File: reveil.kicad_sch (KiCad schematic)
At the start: 24 parts, among them J1 Barrel_Jack_Switch, J2 AudioJack3_SwitchTR, M1 Motor_DC, Q1 2N3904, Q2 IRLB8721PBF

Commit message: Schéma/PCB : isole VBUS du jack J1, alimente le reste de la carte via VSYS
Le jack J1 alimentait directement le net VBUS, partagé avec la broche VBUS
du Pico : branché en même temps que l'USB, les deux 5 V se retrouvaient en
parallèle et le jack pouvait renvoyer du courant vers le PC.

Ajoute D3 (Schottky 1N5822, même référence que D2) entre le jack et un
nouveau rail renommé VSYS, plus C6 (220 µF) en entrée. Tout ce qui était
sur VBUS (MAX7219 U1/U2, moteur, LED, D2) passe sur VSYS, qui alimente le
Pico via sa broche VSYS (39) au lieu de VBUS (40) — VBUS reste réservé à
l'alimentation USB du Pico lui-même.

Met à jour le README (TODO alimentation + table des points de test).

Co-Authored-By: Claude Sonnet 5 <noreply@anthropic.com>
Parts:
- added C6: 220uF, Capacitor_THT:CP_Radial_D7.5mm_P2.50mm, symbol Device:C_Polarized
- added D3: 1N5822, Diode_THT:D_DO-41_SOD81_P10.16mm_Horizontal, symbol Device:D_Schottky
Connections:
- net GND: now also C6.2
- net VSYS: now reaches A1.39 (VSYS)
- net VSYS: now also C5.1, D1.2 (A), D2.1 (K), J2.S, M1.1 (+), C6.1, D3.1 (K)
- removed net VBUS: A1.40 (VBUS), C5.1, D1.2 (A), D2.1 (K), J1.1, J2.S, M1.1 (+)
- new net: D3.2 (A), J1.1

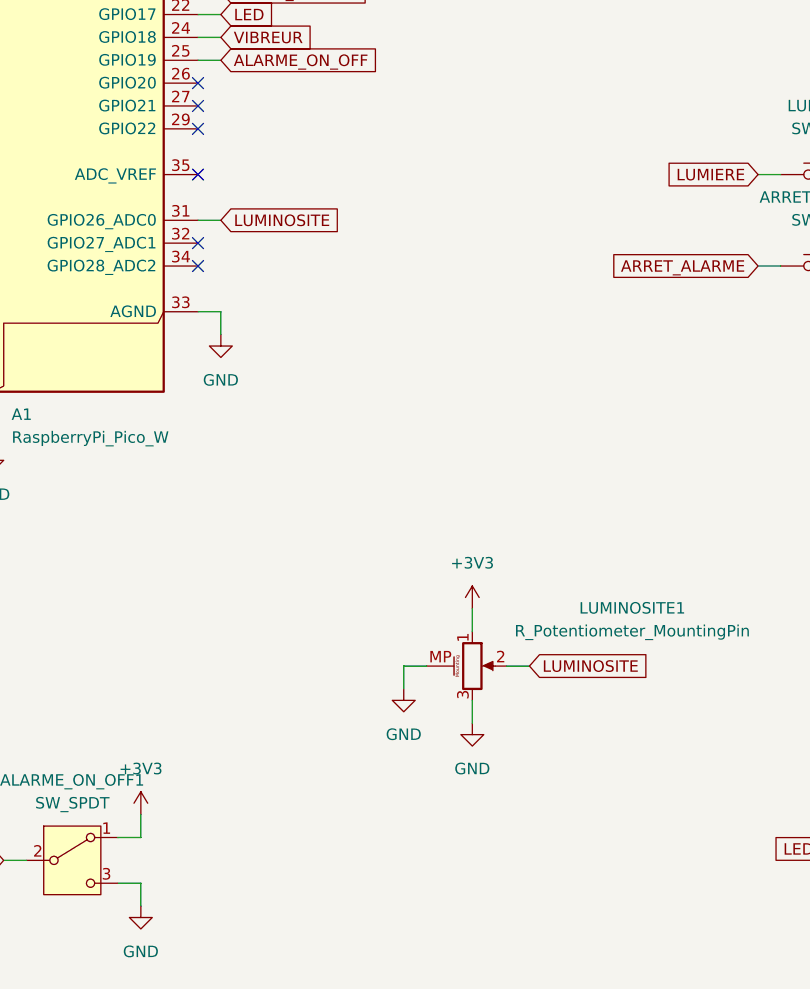
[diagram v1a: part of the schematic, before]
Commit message: Schéma/PCB : découple LUMINOSITE et l'alimente depuis ADC_VREF
Ajoute C7 (100 nF) sur le curseur du potentiomètre LUMINOSITE1, et
reconnecte le haut du pont diviseur sur la broche ADC_VREF du Pico
(auparavant non connectée) au lieu de +3V3, pour une référence ADC plus
propre.

Met à jour le README : coche ce point, et marque le bouton reset et les
filtres RC des encodeurs comme des décisions explicites (pas voulus /
pas nécessaires pour l'instant) plutôt que des TODO ouverts.

Co-Authored-By: Claude Sonnet 5 <noreply@anthropic.com>
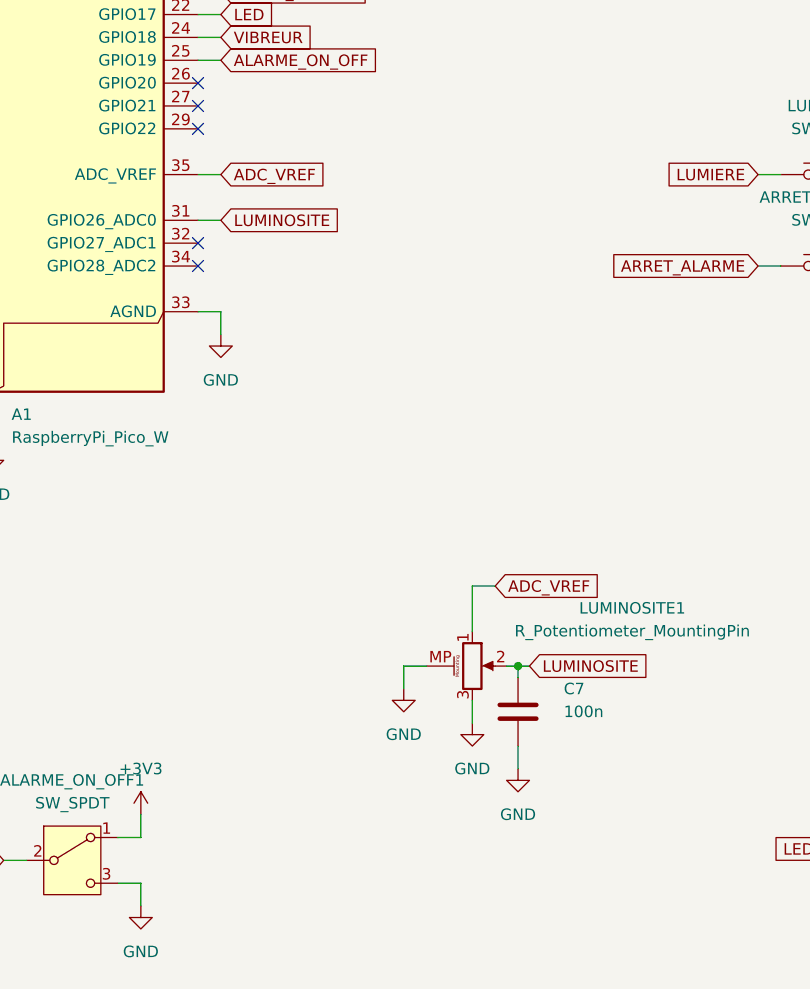
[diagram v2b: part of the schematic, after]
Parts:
- added C7: 100n, Capacitor_THT:C_Disc_D3.0mm_W1.6mm_P2.50mm, symbol Device:C
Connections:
- net +3V3: no longer LUMINOSITE1.1
- net GND: now also C7.2
- net LUMINOSITE: now also C7.1
- net ADC_VREF: now reaches A1.35 (ADC_VREF)
- net ADC_VREF: now also LUMINOSITE1.1
- no-connect marks 13 -> 12
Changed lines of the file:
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@@
 	)
 	(junction
+		(at 140.97 123.19)
+		(diameter 0)
+		(color 0 0 0 0)
+	)
+	(junction
 		(at 185.42 143.51)
 		(diameter 0)
@@
 	)
 	(no_connect
-		(at 105.41 68.58)
-	)
-	(no_connect
 		(at 105.41 60.96)
 	)
@@
 	(wire
 		(pts
+			(xy 105.41 68.58) (xy 107.95 68.58)
+		)
+		(stroke
+			(width 0)
+			(type default)
+		)
+	)
+	(wire
+		(pts
 			(xy 165.1 35.56) (xy 170.18 35.56)
 		)
@@
 	(wire
 		(pts
+			(xy 138.43 114.3) (xy 135.89 114.3)
+		)
+		(stroke
+			(width 0)
+			(type default)
+		)
+	)
+	(wire
+		(pts
 			(xy 233.68 35.56) (xy 238.76 35.56)
 		)
@@
 	(wire
 		(pts
-			(xy 142.24 123.19) (xy 139.7 123.19)
+			(xy 142.24 123.19) (xy 140.97 123.19)
 		)
 		(stroke
@@
 	(wire
 		(pts
+			(xy 135.89 114.3) (xy 135.89 119.38)
+		)
+		(stroke
+			(width 0)
+			(type default)
+		)
+	)
+	(wire
+		(pts
 			(xy 247.65 137.16) (xy 262.89 137.16)
 		)
@@
 	(wire
 		(pts
+			(xy 140.97 123.19) (xy 139.7 123.19)
+		)
+		(stroke
+			(width 0)
+			(type default)
+		)
+	)
+	(wire
+		(pts
 			(xy 254 35.56) (xy 259.08 35.56)
 		)
@@
 	(wire
 		(pts
+			(xy 140.97 132.08) (xy 140.97 134.62)
+		)
+		(stroke
+			(width 0)
+			(type default)
+		)
+	)
+	(wire
+		(pts
 			(xy 57.15 83.82) (xy 59.69 83.82)
 		)
@@
 	(wire
 		(pts
-			(xy 273.05 132.08) (xy 273.05 137.16)
+			(xy 140.97 123.19) (xy 140.97 124.46)
 		)
 		(stroke
@@
 	(wire
 		(pts
-			(xy 57.15 48.26) (xy 59.69 48.26)
+			(xy 273.05 132.08) (xy 273.05 137.16)
 		)
 		(stroke
@@
 	(wire
 		(pts
-			(xy 107.95 55.88) (xy 105.41 55.88)
+			(xy 57.15 48.26) (xy 59.69 48.26)
 		)
 		(stroke
@@
 	(wire
 		(pts
-			(xy 135.89 116.84) (xy 135.89 119.38)
+			(xy 107.95 55.88) (xy 105.41 55.88)
 		)
 		(stroke
@@
 		)
 	)
+	(global_label "ADC_VREF"
+		(shape input)
+		(at 138.43 114.3 0)
+		(fields_autoplaced yes)
+		(effects
+			(font
+				(size 1.27 1.27)
+			)
+			(justify left)
+		)
+		(property "Intersheetrefs" "${INTERSHEET_REFS}"
+			(at 150.6076 114.3 0)
+			(effects
+				(font
+					(size 1.27 1.27)
+				)
+				(justify left)
+				(hide yes)
+			)
+		)
+	)
 	(global_label "HEURE_ALARME_DIN"
 		(shape input)
@@
 		)
 	)
+	(global_label "ADC_VREF"
+		(shape input)
+		(at 107.95 68.58 0)
+		(fields_autoplaced yes)
+		(effects
+			(font
+				(size 1.27 1.27)
+			)
+			(justify left)
+		)
+		(property "Intersheetrefs" "${INTERSHEET_REFS}"
+			(at 120.1276 68.58 0)
+			(effects
+				(font
+					(size 1.27 1.27)
+				)
+				(justify left)
+				(hide yes)
+			)
+		)
+	)
 	(global_label "REGLAGE_DATE_A"
 		(shape input)
@@
 	)
 	(symbol
+		(lib_id "power:GND")
+		(at 140.97 134.62 0)
+		(unit 1)
+		(exclude_from_sim no)
+		(in_bom yes)
+		(on_board yes)
+		(dnp no)
+		(fields_autoplaced yes)
+		(property "Reference" "#PWR017"
+			(at 140.97 140.97 0)
+			(effects
+				(font
+					(size 1.27 1.27)
+				)
+				(hide yes)
+			)
+		)
+		(property "Value" "GND"
+			(at 140.97 139.7 0)
+			(effects
+				(font
+					(size 1.27 1.27)
+				)
+			)
+		)
+		(property "Footprint" ""
+			(at 140.97 134.62 0)
+			(effects
+				(font
+					(size 1.27 1.27)
+				)
+				(hide yes)
+			)
+		)
+		(property "Datasheet" ""
+			(at 140.97 134.62 0)
+			(effects
+				(font
+					(size 1.27 1.27)
+				)
+				(hide yes)
+			)
+		)
+		(property "Description" "Power symbol creates a global label with name \"GND\" , ground"
+			(at 140.97 134.62 0)
+			(effects
+				(font
+					(size 1.27 1.27)
+				)
+				(hide yes)
+			)
+		)
+		(pin "1"
+		)
+		(instances
+			(project "reveil"
+				(path "/6015885c-867c-4e88-9a3e-de8167bfed74"
+					(reference "#PWR017")
+					(unit 1)
+				)
+			)
+		)
+	)
+	(symbol
 		(lib_id "Device:C_Polarized")
 		(at 55.88 123.19 0)
@@
 	)
 	(symbol
-		(lib_id "power:+3V3")
-		(at 135.89 116.84 0)
-		(unit 1)
-		(exclude_from_sim no)
-		(in_bom yes)
-		(on_board yes)
-		(dnp no)
-		(fields_autoplaced yes)
-		(property "Reference" "#PWR017"
-			(at 135.89 120.65 0)
-			(effects
-				(font
-					(size 1.27 1.27)
-				)
-				(hide yes)
-			)
-		)
-		(property "Value" "+3V3"
-			(at 135.89 111.76 0)
-			(effects
-				(font
-					(size 1.27 1.27)
-				)
-			)
-		)
-		(property "Footprint" ""
-			(at 135.89 116.84 0)
-			(effects
-				(font
-					(size 1.27 1.27)
-				)
-				(hide yes)
-			)
-		)
-		(property "Datasheet" ""
-			(at 135.89 116.84 0)
-			(effects
-				(font
-					(size 1.27 1.27)
-				)
-				(hide yes)
-			)
-		)
-		(property "Description" "Power symbol creates a global label with name \"+3V3\""
-			(at 135.89 116.84 0)
-			(effects
-				(font
-					(size 1.27 1.27)
-				)
-				(hide yes)
-			)
-		)
-		(pin "1"
-		)
-		(instances
-			(project "reveil"
-				(path "/6015885c-867c-4e88-9a3e-de8167bfed74"
-					(reference "#PWR017")
-					(unit 1)
-				)
-			)
-		)
-	)
-	(symbol
 		(lib_id "power:GND")
 		(at 240.03 152.4 0)
@@
 					(unit 1)
 				)
+			)
+		)
+	)
+	(symbol
+		(lib_id "Device:C")
+		(at 140.97 128.27 0)
+		(unit 1)
+		(exclude_from_sim no)
+		(in_bom yes)
+		(on_board yes)
+		(dnp no)
+		(fields_autoplaced yes)
+		(property "Reference" "C7"
+			(at 146.05 125.73 0)
+			(effects
+				(font
+					(size 1.27 1.27)
+				)
+				(justify left)
+			)
+		)
+		(property "Value" "100n"
+			(at 146.05 128.27 0)
+			(effects
+				(font
+					(size 1.27 1.27)
+				)
+				(justify left)
+			)
+		)
+		(property "Footprint" "Capacitor_THT:C_Disc_D3.0mm_W1.6mm_P2.50mm"
+			(at 141.9352 124.46 0)
+			(effects
+				(font
+					(size 1.27 1.27)
+				)
+				(hide yes)
+			)
+		)
+		(property "Datasheet" "~"
+			(at 140.97 128.27 0)
+			(effects
+				(font
+					(size 1.27 1.27)
+				)
+				(hide yes)
+			)
+		)
+		(property "Description" "Unpolarized capacitor"
+			(at 140.97 128.27 0)
+			(effects
+				(font
+					(size 1.27 1.27)
+				)
+				(hide yes)
+			)
+		)
+		(pin "1"
+		)
+		(pin "2"
+		)
+		(instances
+			(project "reveil"
+				(path "/6015885c-867c-4e88-9a3e-de8167bfed74"
+					(reference "C7")
+					(unit 1)
+				)
